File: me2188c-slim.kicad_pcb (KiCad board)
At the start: 2 copper layers, 17 x 17 mm, 5 parts, among them J1 Conn_01x04_Male, U1 ME2188

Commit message: routed
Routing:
- net Net-(C1-Pad1): track 0.00 -> 23.3 mm
- net Net-(U1-Pad2): track 0.00 -> 21.8 mm
- net GND: track 0.00 -> 17.5 mm
- net Net-(U1-Pad5): track 0.00 -> 5.80 mm
- net Net-(U1-Pad1): track 0.00 -> 3.15 mm
- added copper zone on B.Cu, net GND
- added copper zone on F.Cu, net GND
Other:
- board text added: "CE"
- board text added: "GND"
- board text added: "VIN"
- board text added: "VOUT"
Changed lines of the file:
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@@
   (gr_line (start 100 100) (end 117 100) (layer "Edge.Cuts") (width 0.1))
   (gr_line (start 100 117) (end 117 117) (layer "Edge.Cuts") (width 0.1))
+  (gr_text "VOUT" (at 105.156 110.236 -90) (layer "B.SilkS")
+    (effects (font (size 1.5 1.5) (thickness 0.3)) (justify mirror))
+  )
+  (gr_text "CE" (at 107.696 111.76 -90) (layer "B.SilkS")
+    (effects (font (size 1.5 1.5) (thickness 0.3)) (justify mirror))
+  )
+  (gr_text "GND" (at 112.776 111.252 -90) (layer "B.SilkS")
+    (effects (font (size 1.5 1.5) (thickness 0.3)) (justify mirror))
+  )
+  (gr_text "VIN" (at 109.728 111.252 -90) (layer "B.SilkS")
+    (effects (font (size 1.5 1.5) (thickness 0.3)) (justify mirror))
+  )
+  (segment (start 112.9047 107.2153) (end 110.632 107.2153) (width 0.25) (layer "F.Cu") (net 1))
+  (segment (start 111.4113 115.5834) (end 111.4113 115.216) (width 0.25) (layer "F.Cu") (net 1))
+  (segment (start 116.223 110.5336) (end 116.223 113.4522) (width 0.25) (layer "F.Cu") (net 1))
+  (segment (start 110.632 104.14) (end 110.632 107.2153) (width 0.25) (layer "F.Cu") (net 1))
+  (segment (start 113.2839 116.3913) (end 112.2192 116.3913) (width 0.25) (layer "F.Cu") (net 1))
+  (segment (start 112.9047 107.2153) (end 116.223 110.5336) (width 0.25) (layer "F.Cu") (net 1))
+  (segment (start 112.2192 116.3913) (end 111.4113 115.5834) (width 0.25) (layer "F.Cu") (net 1))
+  (segment (start 116.223 113.4522) (end 113.2839 116.3913) (width 0.25) (layer "F.Cu") (net 1))
+  (segment (start 110.236 115.216) (end 111.4113 115.216) (width 0.25) (layer "F.Cu") (net 1))
+  (segment (start 114.608 105.512) (end 112.9047 107.2153) (width 0.25) (layer "F.Cu") (net 1))
+  (segment (start 102.516 111.912) (end 103.8897 110.5383) (width 0.25) (layer "F.Cu") (net 3))
+  (segment (start 112.776 113.744) (end 112.776 115.216) (width 0.25) (layer "F.Cu") (net 3))
+  (segment (start 109.4495 110.1591) (end 109.662 109.9466) (width 0.25) (layer "F.Cu") (net 3))
+  (segment (start 114.608 111.912) (end 112.9052 113.6148) (width 0.25) (layer "F.Cu") (net 3))
+  (segment (start 103.8897 110.5383) (end 109.0703 110.5383) (width 0.25) (layer "F.Cu") (net 3))
+  (segment (start 109.662 109.394) (end 109.662 109.9466) (width 0.25) (layer "F.Cu") (net 3))
+  (segment (start 112.9052 113.6148) (end 112.776 113.744) (width 0.25) (layer "F.Cu") (net 3))
+  (segment (start 109.4495 110.1591) (end 112.9052 113.6148) (width 0.25) (layer "F.Cu") (net 3))
+  (segment (start 109.0703 110.5383) (end 109.4495 110.1591) (width 0.25) (layer "F.Cu") (net 3))
+  (segment (start 107.1799 116.4319) (end 108.1732 116.4319) (width 0.25) (layer "F.Cu") (net 4))
+  (segment (start 106.3313 115.216) (end 106.3313 115.5833) (width 0.25) (layer "F.Cu") (net 4))
+  (segment (start 105.156 115.216) (end 106.3313 115.216) (width 0.25) (layer "F.Cu") (net 4))
+  (segment (start 106.3313 115.5833) (end 107.1799 116.4319) (width 0.25) (layer "F.Cu") (net 4))
+  (segment (start 108.8805 115.7246) (end 108.8805 113.3678) (width 0.25) (layer "F.Cu") (net 4))
+  (segment (start 100.9143 107.1137) (end 100.9143 113.1023) (width 0.25) (layer "F.Cu") (net 4))
+  (segment (start 102.516 105.512) (end 100.9143 107.1137) (width 0.25) (layer "F.Cu") (net 4))
+  (segment (start 103.028 115.216) (end 105.156 115.216) (width 0.25) (layer "F.Cu") (net 4))
+  (segment (start 108.712 112.094) (end 108.712 113.1993) (width 0.25) (layer "F.Cu") (net 4))
+  (segment (start 108.1732 116.4319) (end 108.8805 115.7246) (width 0.25) (layer "F.Cu") (net 4))
+  (segment (start 108.8805 113.3678) (end 108.712 113.1993) (width 0.25) (layer "F.Cu") (net 4))
+  (segment (start 100.9143 113.1023) (end 103.028 115.216) (width 0.25) (layer "F.Cu") (net 4))
+  (segment (start 107.6654 108.2887) (end 106.592 107.2153) (width 0.25) (layer "F.Cu") (net 5))
+  (segment (start 107.762 108.2887) (end 107.6654 108.2887) (width 0.25) (layer "F.Cu") (net 5))
+  (segment (start 106.592 104.14) (end 106.592 107.2153) (width 0.25) (layer "F.Cu") (net 5))
+  (segment (start 107.762 109.394) (end 107.762 108.2887) (width 0.25) (layer "F.Cu") (net 5))
+  (segment (start 107.696 115.216) (end 107.696 114.0407) (width 0.25) (layer "F.Cu") (net 6))
+  (segment (start 107.762 112.094) (end 107.762 113.9747) (width 0.25) (layer "F.Cu") (net 6))
+  (segment (start 107.762 113.9747) (end 107.696 114.0407) (width 0.25) (layer "F.Cu") (net 6))
+  (zone (net 3) (net_name "GND") (layers F&B.Cu) (hatch edge 0.508)
+    (connect_pads (clearance 0.508))
+    (min_thickness 0.254) (filled_areas_thickness no)
+    (fill yes (thermal_gap 0.508) (thermal_bridge_width 0.508))
+    (polygon
+      (pts
+        (xy 117.348 117.348)
+        (xy 99.568 117.348)
+        (xy 99.568 99.568)
+        (xy 117.348 99.568)
+      )
+    )
+  )
 )

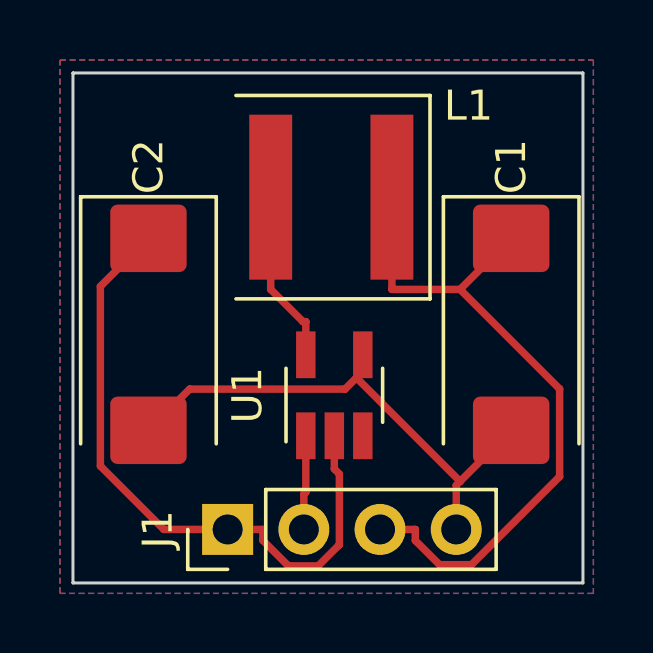
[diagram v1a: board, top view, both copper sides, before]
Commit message: inductor footprint corrected and capacitors added
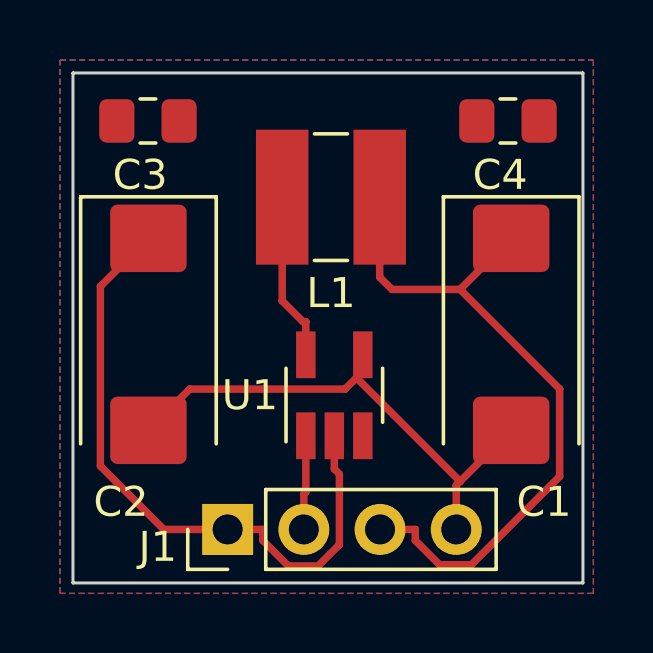
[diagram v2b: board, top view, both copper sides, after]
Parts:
- added C3: 100nF, Capacitor_SMD:C_0805_2012Metric_Pad1.18x1.45mm_HandSolder, F.Cu at (102.5, 101.6)
- added C4: 100nF, Capacitor_SMD:C_0805_2012Metric_Pad1.18x1.45mm_HandSolder, F.Cu at (114.5, 101.6)
- C1: value C_Polarized -> 10uF
- C2: value C_Polarized -> 100uF
- L1: footprint Inductor_SMD:L_Coilcraft_XAL60xx_6.36x6.56mm -> Inductor_SMD:L_Ferrocore_DLG-0403

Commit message: board routed
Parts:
- moved C3 0.20 mm to (102.5, 101.8)
- moved C4 0.20 mm to (114.5, 101.8)
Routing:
- net GND: track 17.5 -> 0.00 mm
- net Net-(C1-Pad1): track 23.4 -> 18.9 mm
- net Net-(C2-Pad1): track 21.8 -> 19.3 mm
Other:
- board text added: "ME2188C"
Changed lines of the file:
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@@
   )
   (footprint "Capacitor_SMD:C_0805_2012Metric_Pad1.18x1.45mm_HandSolder" (layer "F.Cu")
-    (at 114.5 101.6)
+    (at 114.5 101.8)
     (descr "Capacitor SMD 0805 (2012 Metric), square (rectangular) end terminal, IPC_7351 nominal with elongated pad for handsoldering. (Body size source: IPC-SM-782 page 76, https://www.pcb-3d.com/wordpress/wp-content/uploads/ipc-sm-782a_amendment_1_and_2.pdf, https://docs.google.com/spreadsheets/d/1BsfQQcO9C6DZCsRaXUlFlo91Tg2WpOkGARC1WS5S8t0/edit?usp=sharing), generated with kicad-footprint-generator")
     (tags "capacitor handsolder")
@@
     (property "Sheetname" "")
     (attr smd)
-    (fp_text reference "C4" (at -0.261252 1.8) (layer "F.SilkS")
+    (fp_text reference "C4" (at -0.261252 1.7) (layer "F.SilkS")
       (effects (font (size 1 1) (thickness 0.15)))
     )
@@
   )
   (footprint "Capacitor_SMD:C_0805_2012Metric_Pad1.18x1.45mm_HandSolder" (layer "F.Cu")
-    (at 102.5 101.6)
+    (at 102.5 101.8)
     (descr "Capacitor SMD 0805 (2012 Metric), square (rectangular) end terminal, IPC_7351 nominal with elongated pad for handsoldering. (Body size source: IPC-SM-782 page 76, https://www.pcb-3d.com/wordpress/wp-content/uploads/ipc-sm-782a_amendment_1_and_2.pdf, https://docs.google.com/spreadsheets/d/1BsfQQcO9C6DZCsRaXUlFlo91Tg2WpOkGARC1WS5S8t0/edit?usp=sharing), generated with kicad-footprint-generator")
     (tags "capacitor handsolder")
@@
     (property "Sheetname" "")
     (attr smd)
-    (fp_text reference "C3" (at -0.261252 1.8) (layer "F.SilkS")
+    (fp_text reference "C3" (at -0.261252 1.7) (layer "F.SilkS")
       (effects (font (size 1 1) (thickness 0.15)))
     )
@@
     (effects (font (size 1.5 1.5) (thickness 0.3)) (justify mirror))
   )
+  (gr_text "ME2188C" (at 101.6 109.22 -90) (layer "B.SilkS")
+    (effects (font (size 1 1) (thickness 0.15)) (justify mirror))
+  )
   (gr_text "CE" (at 107.696 111.76 -90) (layer "B.SilkS")
     (effects (font (size 1.5 1.5) (thickness 0.3)) (justify mirror))
@@
     (effects (font (size 1.5 1.5) (thickness 0.3)) (justify mirror))
   )
-  (gr_text "VIN" (at 109.728 111.252 -90) (layer "B.SilkS")
-    (effects (font (size 1.5 1.5) (thickness 0.3)) (justify mirror))
-  )
-  (segment (start 112.9047 107.2153) (end 110.632 107.2153) (width 0.25) (layer "F.Cu") (net 1))
-  (segment (start 111.4113 115.5834) (end 111.4113 115.216) (width 0.25) (layer "F.Cu") (net 1))
-  (segment (start 116.223 110.5336) (end 116.223 113.4522) (width 0.25) (layer "F.Cu") (net 1))
-  (segment (start 113.2839 116.3913) (end 112.2192 116.3913) (width 0.25) (layer "F.Cu") (net 1))
-  (segment (start 112.9047 107.2153) (end 116.223 110.5336) (width 0.25) (layer "F.Cu") (net 1))
-  (segment (start 110.225 106.8083) (end 110.225 104.14) (width 0.25) (layer "F.Cu") (net 1))
-  (segment (start 112.2192 116.3913) (end 111.4113 115.5834) (width 0.25) (layer "F.Cu") (net 1))
-  (segment (start 110.632 107.2153) (end 110.225 106.8083) (width 0.25) (layer "F.Cu") (net 1))
-  (segment (start 116.223 113.4522) (end 113.2839 116.3913) (width 0.25) (layer "F.Cu") (net 1))
-  (segment (start 110.236 115.216) (end 111.4113 115.216) (width 0.25) (layer "F.Cu") (net 1))
-  (segment (start 114.608 105.512) (end 112.9047 107.2153) (width 0.25) (layer "F.Cu") (net 1))
-  (segment (start 102.516 111.912) (end 103.8897 110.5383) (width 0.25) (layer "F.Cu") (net 3))
-  (segment (start 112.776 113.744) (end 112.776 115.216) (width 0.25) (layer "F.Cu") (net 3))
-  (segment (start 109.4495 110.1591) (end 109.662 109.9466) (width 0.25) (layer "F.Cu") (net 3))
-  (segment (start 114.608 111.912) (end 112.9052 113.6148) (width 0.25) (layer "F.Cu") (net 3))
-  (segment (start 103.8897 110.5383) (end 109.0703 110.5383) (width 0.25) (layer "F.Cu") (net 3))
-  (segment (start 109.662 109.394) (end 109.662 109.9466) (width 0.25) (layer "F.Cu") (net 3))
-  (segment (start 112.9052 113.6148) (end 112.776 113.744) (width 0.25) (layer "F.Cu") (net 3))
-  (segment (start 109.4495 110.1591) (end 112.9052 113.6148) (width 0.25) (layer "F.Cu") (net 3))
-  (segment (start 109.0703 110.5383) (end 109.4495 110.1591) (width 0.25) (layer "F.Cu") (net 3))
-  (segment (start 107.1799 116.4319) (end 108.1732 116.4319) (width 0.25) (layer "F.Cu") (net 4))
-  (segment (start 106.3313 115.216) (end 106.3313 115.5833) (width 0.25) (layer "F.Cu") (net 4))
-  (segment (start 105.156 115.216) (end 106.3313 115.216) (width 0.25) (layer "F.Cu") (net 4))
-  (segment (start 106.3313 115.5833) (end 107.1799 116.4319) (width 0.25) (layer "F.Cu") (net 4))
-  (segment (start 108.8805 115.7246) (end 108.8805 113.3678) (width 0.25) (layer "F.Cu") (net 4))
-  (segment (start 100.9143 107.1137) (end 100.9143 113.1023) (width 0.25) (layer "F.Cu") (net 4))
-  (segment (start 102.516 105.512) (end 100.9143 107.1137) (width 0.25) (layer "F.Cu") (net 4))
-  (segment (start 103.028 115.216) (end 105.156 115.216) (width 0.25) (layer "F.Cu") (net 4))
-  (segment (start 108.712 112.094) (end 108.712 113.1993) (width 0.25) (layer "F.Cu") (net 4))
-  (segment (start 108.1732 116.4319) (end 108.8805 115.7246) (width 0.25) (layer "F.Cu") (net 4))
-  (segment (start 108.8805 113.3678) (end 108.712 113.1993) (width 0.25) (layer "F.Cu") (net 4))
-  (segment (start 100.9143 113.1023) (end 103.028 115.216) (width 0.25) (layer "F.Cu") (net 4))
-  (segment (start 107.696 115.216) (end 107.696 114.0407) (width 0.25) (layer "F.Cu") (net 5))
-  (segment (start 107.762 112.094) (end 107.762 113.9747) (width 0.25) (layer "F.Cu") (net 5))
-  (segment (start 107.762 113.9747) (end 107.696 114.0407) (width 0.25) (layer "F.Cu") (net 5))
-  (segment (start 107.762 108.2887) (end 107.6654 108.2887) (width 0.25) (layer "F.Cu") (net 6))
-  (segment (start 107.762 109.394) (end 107.762 108.2887) (width 0.25) (layer "F.Cu") (net 6))
-  (segment (start 106.975 107.5983) (end 106.975 104.14) (width 0.25) (layer "F.Cu") (net 6))
-  (segment (start 107.6654 108.2887) (end 106.975 107.5983) (width 0.25) (layer "F.Cu") (net 6))
+  (gr_text "VIN" (at 110.236 111.252 -90) (layer "B.SilkS")
+    (effects (font (size 1.5 1.5) (thickness 0.3)) (justify mirror))
+  )
+  (segment (start 111.4251 104.14) (end 112.7813 105.4962) (width 0.25) (layer "F.Cu") (net 1))
+  (segment (start 112.7813 111.4956) (end 110.236 114.0409) (width 0.25) (layer "F.Cu") (net 1))
+  (segment (start 112.7813 105.512) (end 114.608 105.512) (width 0.25) (layer "F.Cu") (net 1))
+  (segment (start 113.4625 101.8) (end 111.4251 103.8374) (width 0.25) (layer "F.Cu") (net 1))
+  (segment (start 112.7813 105.4962) (end 112.7813 105.512) (width 0.25) (layer "F.Cu") (net 1))
+  (segment (start 111.4251 103.8374) (end 111.4251 104.14) (width 0.25) (layer "F.Cu") (net 1))
+  (segment (start 110.236 115.216) (end 110.236 114.0409) (width 0.25) (layer "F.Cu") (net 1))
+  (segment (start 110.225 104.14) (end 111.4251 104.14) (width 0.25) (layer "F.Cu") (net 1))
+  (segment (start 112.7813 105.512) (end 112.7813 111.4956) (width 0.25) (layer "F.Cu") (net 1))
+  (segment (start 102.516 105.7236) (end 107.5156 110.7231) (width 0.25) (layer "F.Cu") (net 4))
+  (segment (start 105.156 113.0827) (end 105.156 115.216) (width 0.25) (layer "F.Cu") (net 4))
+  (segment (start 107.5156 110.7231) (end 105.156 113.0827) (width 0.25) (layer "F.Cu") (net 4))
+  (segment (start 107.7813 110.9889) (end 108.712 110.9889) (width 0.25) (layer "F.Cu") (net 4))
+  (segment (start 108.712 112.094) (end 108.712 110.9889) (width 0.25) (layer "F.Cu") (net 4))
+  (segment (start 107.5156 110.7231) (end 107.7813 110.9889) (width 0.25) (layer "F.Cu") (net 4))
+  (segment (start 101.4625 101.8) (end 102.516 102.8535) (width 0.25) (layer "F.Cu") (net 4))
+  (segment (start 102.516 102.8535) (end 102.516 105.512) (width 0.25) (layer "F.Cu") (net 4))
+  (segment (start 102.516 105.512) (end 102.516 105.7236) (width 0.25) (layer "F.Cu") (net 4))
+  (segment (start 107.762 112.094) (end 107.762 113.9749) (width 0.25) (layer "F.Cu") (net 5))
+  (segment (start 107.696 115.216) (end 107.696 114.0409) (width 0.25) (layer "F.Cu") (net 5))
+  (segment (start 107.762 113.9749) (end 107.696 114.0409) (width 0.25) (layer "F.Cu") (net 5))
+  (segment (start 106.975 106.7151) (end 107.762 107.5021) (width 0.25) (layer "F.Cu") (net 6))
+  (segment (start 106.975 104.14) (end 106.975 106.7151) (width 0.25) (layer "F.Cu") (net 6))
+  (segment (start 107.762 107.5021) (end 107.762 109.394) (width 0.25) (layer "F.Cu") (net 6))
   (zone (net 3) (net_name "GND") (layers F&B.Cu) (hatch edge 0.508)
-    (connect_pads (clearance 0.508))
+    (connect_pads (clearance 0.254))
     (min_thickness 0.254) (filled_areas_thickness no)
-    (fill (thermal_gap 0.508) (thermal_bridge_width 0.508))
+    (fill yes (thermal_gap 0.508) (thermal_bridge_width 0.508))
     (polygon
       (pts

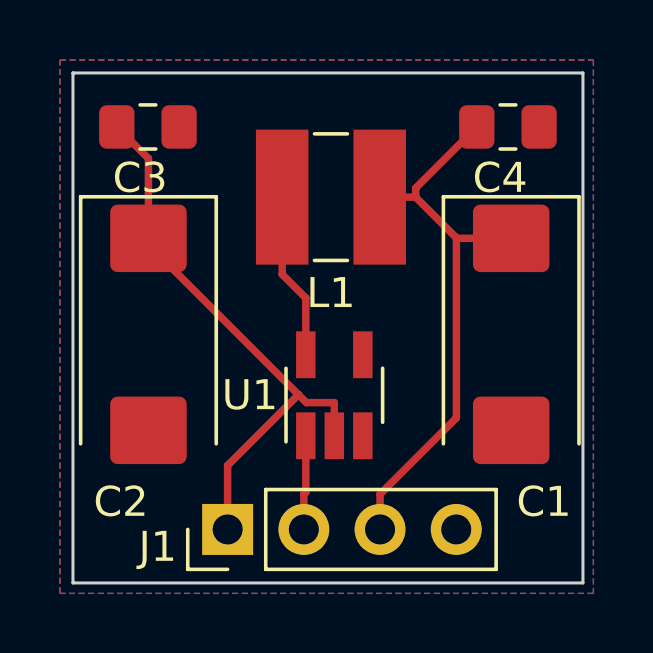
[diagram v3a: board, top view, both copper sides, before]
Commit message: shrinked and routed
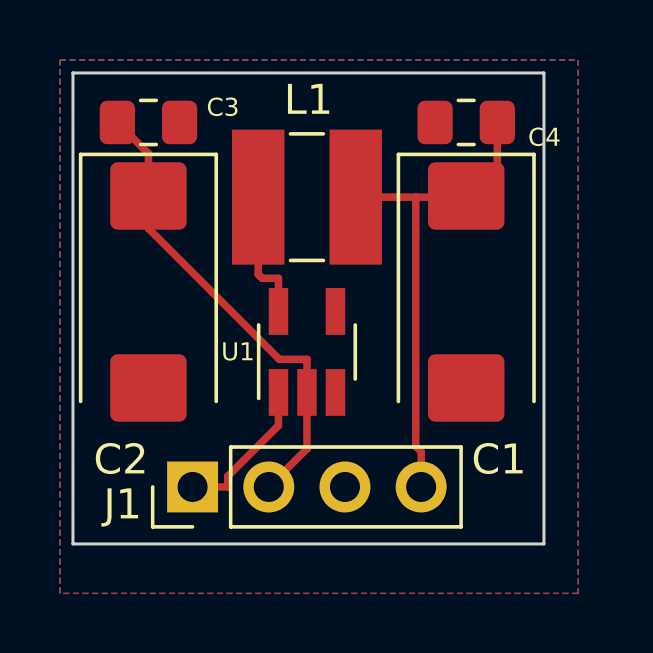
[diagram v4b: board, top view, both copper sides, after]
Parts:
- L1: value L -> 22uH
- moved C1 2.06 mm to (113.1, 107.3)
- moved J1 1.84 mm to (104.0, 113.8)
- moved U1 1.71 mm to (107.8, 109.3)
- moved C2 1.41 mm to (102.5, 107.3)
- moved C4 1.40 mm to (113.1, 101.7), turned to 180 degrees
- moved L1 0.80 mm to (107.8, 104.1)
- moved C3 0.15 mm to (102.5, 101.7)
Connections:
- J1 pad 1: Net-(C2-Pad1) -> Net-(U1-Pad1)
- J1 pad 2: Net-(J1-Pad2) -> Net-(C2-Pad1)
- J1 pad 3: Net-(C1-Pad1) -> GND
- J1 pad 4: GND -> Net-(C1-Pad1)
- U1 pad 1: Net-(J1-Pad2) -> Net-(U1-Pad1)
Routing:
- net Net-(U1-Pad1): track 0.00 -> 5.02 mm
- net Net-(C2-Pad1): track 19.3 -> 15.8 mm
- net Net-(J1-Pad2): track 3.15 -> 0.00 mm
- net Net-(C1-Pad1): track 18.9 -> 16.3 mm
- net Net-(L1-Pad2): track 5.58 -> 4.41 mm
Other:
- board size 17 x 17 mm -> 15.7 x 15.7 mm

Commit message: OSHW logo added
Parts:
- added REF**: OSHW-Symbol_6.7x6mm_SilkScreen, Symbol:OSHW-Symbol_6.7x6mm_SilkScreen, B.Cu at (111.8, 104.1)
